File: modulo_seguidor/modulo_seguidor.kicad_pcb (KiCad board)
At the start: 12 copper layers, 100 x 50 mm, 12 parts, among them J1 Battery, J4 Motor Izquierdo, J5 Motor Derecho, J6 puerto sensores, SW1 SW_Push, U1 LM7806_TO220

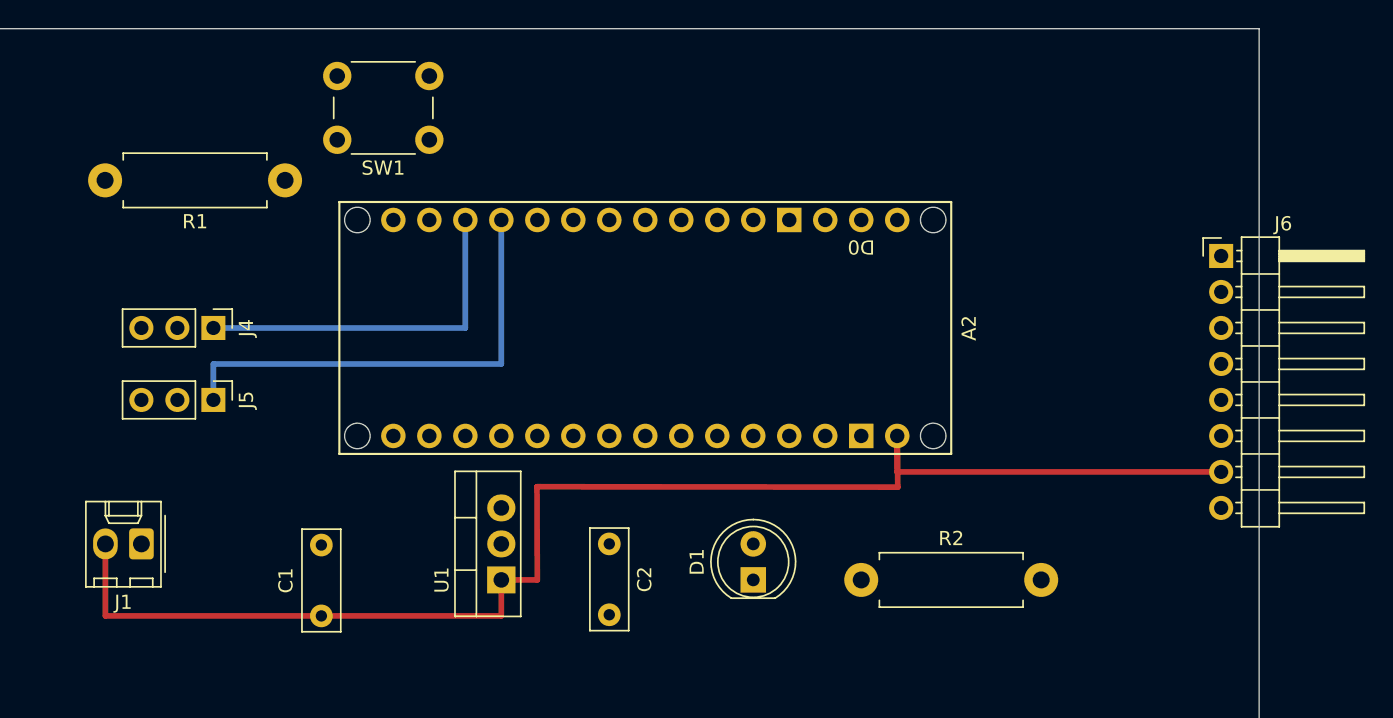
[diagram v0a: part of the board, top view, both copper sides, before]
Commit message: refactor: Cambio las conexiones en los pines del modulo seguidor para compactar la pcb
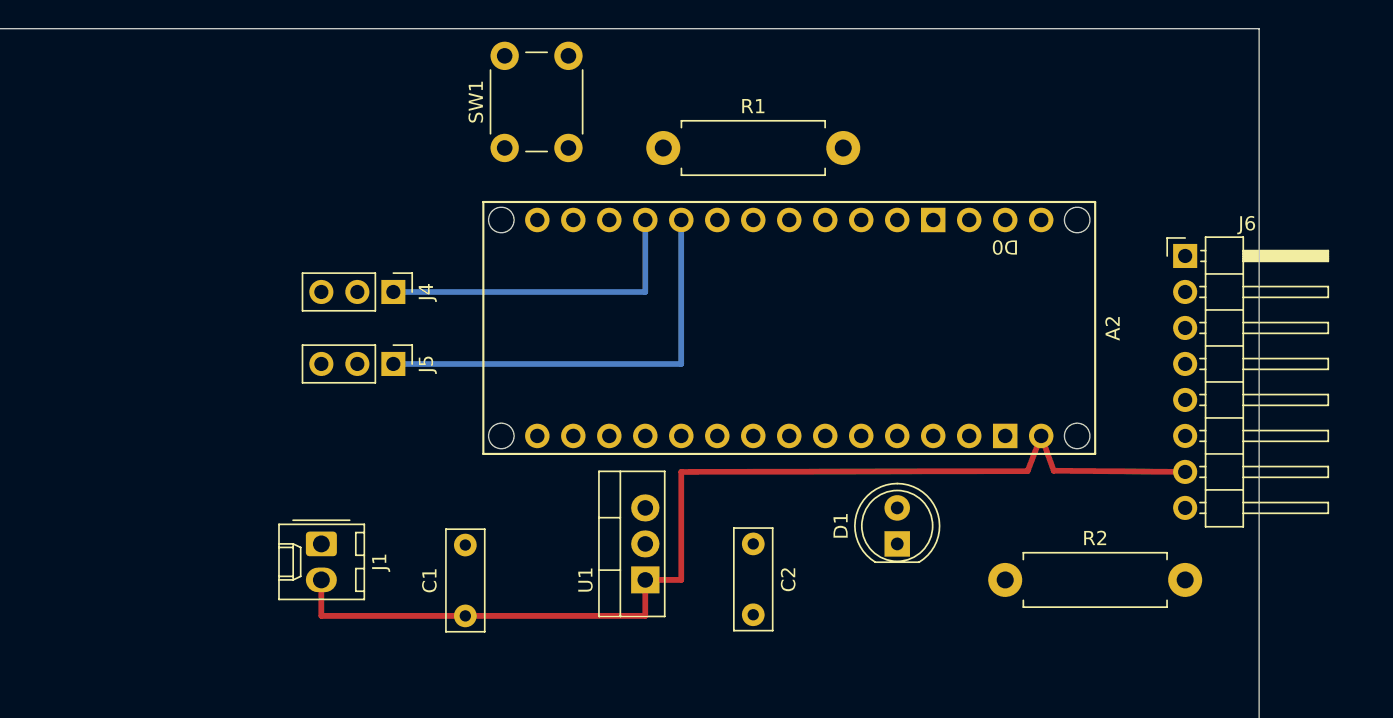
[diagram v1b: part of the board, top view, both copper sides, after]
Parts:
- moved R1 26.8 mm to (108.0, 58.4), turned to 0 degrees
- moved J4 13.0 mm to (88.9, 68.6)
- moved J5 13.0 mm to (88.9, 73.7)
- moved J1 12.7 mm to (83.8, 86.4), turned to -90 degrees
- moved D1 10.5 mm to (124.5, 86.4)
- moved C1 10.2 mm to (94.0, 91.4)
- moved R2 10.2 mm to (132.1, 88.9)
- moved U1 10.2 mm to (106.7, 88.9)
- moved A2 10.2 mm to (95.2, 71.1)
- moved C2 10.2 mm to (114.3, 86.4)
- moved SW1 5.35 mm to (96.8, 58.4), turned to 90 degrees
- moved J6 2.54 mm to (144.8, 66.0)
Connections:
- A2 pad D10: /PWM_IZQ -> /Boton_encendido
- A2 pad D2: /Boton_encendido -> /Sensor6
- A2 pad D3: /Sensor6 -> /Sensor5
- A2 pad D4: /Sensor5 -> /Sensor4
- A2 pad D5: /Sensor4 -> /Sensor3
- A2 pad D6: /Sensor3 -> /Sensor2
- A2 pad D7: /Sensor2 -> /Sensor1
- A2 pad D8: /Sensor1 -> /PWM_DER
- A2 pad D9: /PWM_DER -> /PWM_IZQ
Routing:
- net GND: track 174.9 -> 137.9 mm
- net /Boton_encendido: track 44.6 -> 18.3 mm
- net VCC: track 99.2 -> 77.1 mm
- net /Sensor5: track 42.3 -> 27.0 mm
- net /Sensor6: track 38.1 -> 22.9 mm
- net /Sensor3: track 50.1 -> 35.1 mm
- net /Sensor2: track 54.1 -> 39.2 mm
- net /Sensor4: track 46.1 -> 31.2 mm
- net /Sensor1: track 58.0 -> 43.1 mm
- net Net-(D1-K): track 7.62 -> 10.2 mm
- net Net-(D1-A): track 7.62 -> 5.08 mm
- net /PWM_IZQ: track 25.4 -> 22.9 mm
- net /PWM_DER: track 33.0 -> 30.5 mm
- net +5V: track 60.9 -> 62.6 mm

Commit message: refactor(modulo_seguidor): Intercambio dos pines para hacer los cables más cortos
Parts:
- moved SW1 2.59 mm to (99.3, 58.4)
- moved R1 1.17 mm to (109.1, 58.3)
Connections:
- A2 pad D10: /Boton_encendido -> /PWM_IZQ
- A2 pad D8: /PWM_DER -> /Boton_encendido
- A2 pad D9: /PWM_IZQ -> /PWM_DER
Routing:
- net +5V: track 62.6 -> 65.2 mm
- net /PWM_IZQ: track 22.9 -> 20.3 mm
- net /PWM_DER: track 30.5 -> 27.9 mm
- net /Boton_encendido: track 18.3 -> 17.0 mm
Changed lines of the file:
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@@
 			(layers "*.Cu" "*.Mask")
 			(remove_unused_layers no)
-			(net 22 "/PWM_DER")
+			(net 8 "/Boton_encendido")
 			(pinfunction "D8")
 			(pintype "bidirectional")
@@
 			(layers "*.Cu" "*.Mask")
 			(remove_unused_layers no)
-			(net 4 "/PWM_IZQ")
+			(net 22 "/PWM_DER")
 			(pinfunction "D9")
 			(pintype "bidirectional")
@@
 			(layers "*.Cu" "*.Mask")
 			(remove_unused_layers no)
-			(net 8 "/Boton_encendido")
+			(net 4 "/PWM_IZQ")
 			(pinfunction "D10")
 			(pintype "bidirectional")
@@
 	(footprint "Resistor_THT:R_Axial_DIN0411_L9.9mm_D3.6mm_P12.70mm_Horizontal"
 		(layer "F.Cu")
-		(at 107.95 58.42)
+		(at 109.109289 58.262866)
 		(descr "Resistor, Axial_DIN0411 series, Axial, Horizontal, pin pitch=12.7mm, 1W, length*diameter=9.9*3.6mm^2")
 		(tags "Resistor Axial_DIN0411 series Axial Horizontal pin pitch 12.7mm 1W length 9.9mm diameter 3.6mm")
 		(property "Reference" "R1"
-			(at 6.35 -2.92 360)
+			(at 6.35 -2.92 0)
 			(layer "F.SilkS")
 			(effects
@@
 		)
 		(property "Value" "1k"
-			(at 6.35 2.92 360)
+			(at 6.35 2.92 0)
 			(layer "F.Fab")
 			(effects
@@
 		)
 		(fp_text user "${REFERENCE}"
-			(at 6.35 0 360)
+			(at 6.35 0 0)
 			(layer "F.Fab")
 			(effects
@@
 	(footprint "Button_Switch_THT:SW_PUSH_6mm"
 		(layer "F.Cu")
-		(at 96.756469 58.416841 90)
+		(at 99.35 58.416841 90)
 		(descr "Generic 6mm SW tactile push button")
 		(tags "tact sw push 6mm")
@@
 	)
 	(segment
-		(start 106.68 68.58)
-		(end 106.68 63.5)
+		(start 104.14 68.58)
+		(end 104.14 63.5)
 		(width 0.4)
 		(layer "B.Cu")
@@
 	(segment
 		(start 88.9 68.58)
-		(end 106.68 68.58)
+		(end 104.14 68.58)
 		(width 0.4)
 		(layer "B.Cu")
@@
 	)
 	(segment
-		(start 101.256469 58.416841)
-		(end 101.256469 51.916841)
-		(width 0.4)
-		(layer "In7.Cu")
-		(net 8)
-	)
-	(segment
-		(start 104.14 58.42)
-		(end 101.256469 58.416841)
-		(width 0.4)
-		(layer "In7.Cu")
-		(net 8)
-	)
-	(segment
-		(start 107.95 58.42)
-		(end 104.14 58.431505)
+		(start 109.109289 58.262866)
+		(end 109.22 63.5)
 		(width 0.4)
 		(layer "In7.Cu")
@@
 	)
 	(segment
-		(start 104.14 60.96)
-		(end 104.14 58.42)
+		(start 103.85 58.416841)
+		(end 109.109289 58.262866)
 		(width 0.4)
 		(layer "In7.Cu")
@@
 	)
 	(segment
-		(start 104.14 63.5)
-		(end 104.14 60.96)
+		(start 103.85 51.916841)
+		(end 103.85 58.416841)
 		(width 0.4)
 		(layer "In7.Cu")
@@
 	)
 	(segment
-		(start 109.22 73.66)
-		(end 109.22 63.5)
+		(start 88.9 73.66)
+		(end 106.68 73.66)
 		(width 0.4)
 		(layer "B.Cu")
@@
 	)
 	(segment
-		(start 88.9 73.66)
-		(end 109.22 73.66)
+		(start 106.68 73.66)
+		(end 106.68 63.5)
 		(width 0.4)
 		(layer "B.Cu")
@@
 	)
 	(segment
-		(start 96.756469 51.916841)
-		(end 96.756469 58.416841)
+		(start 127 76.2)
+		(end 127 78.74)
 		(width 0.4)
 		(layer "In10.Cu")
@@
 	)
 	(segment
-		(start 96.756469 58.416841)
-		(end 93.98 58.42)
+		(start 93.98 58.42)
+		(end 93.98 76.2)
 		(width 0.4)
 		(layer "In10.Cu")
@@
 	)
 	(segment
-		(start 93.98 58.42)
-		(end 93.98 76.2)
+		(start 99.35 51.916841)
+		(end 99.35 58.416841)
 		(width 0.4)
 		(layer "In10.Cu")
@@
 	)
 	(segment
-		(start 93.98 76.2)
-		(end 127 76.2)
+		(start 99.35 58.416841)
+		(end 93.98 58.42)
 		(width 0.4)
 		(layer "In10.Cu")
@@
 	)
 	(segment
-		(start 127 76.2)
-		(end 127 78.74)
+		(start 93.98 76.2)
+		(end 127 76.2)
 		(width 0.4)
 		(layer "In10.Cu")

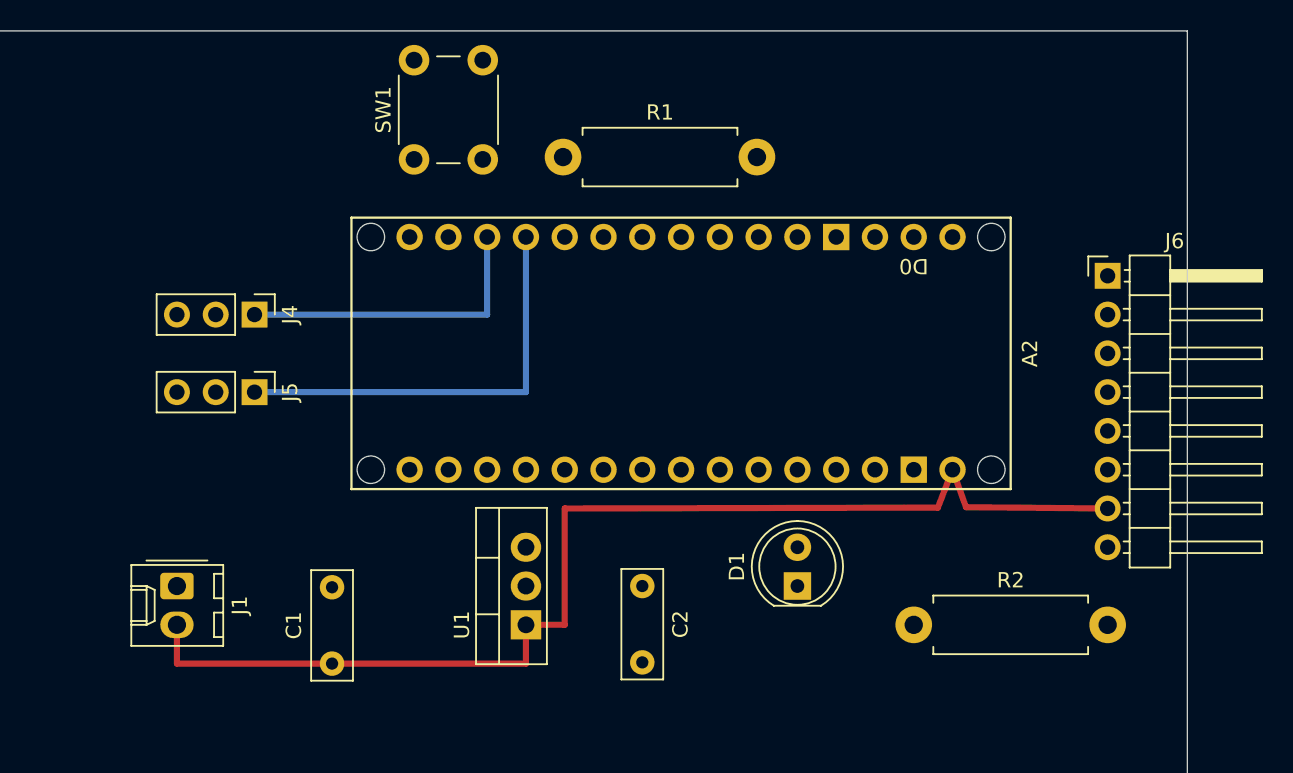
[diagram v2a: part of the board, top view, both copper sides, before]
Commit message: feat(modulo_seguidor): Agrego partes no perforadas y lo referencio en la documentacion
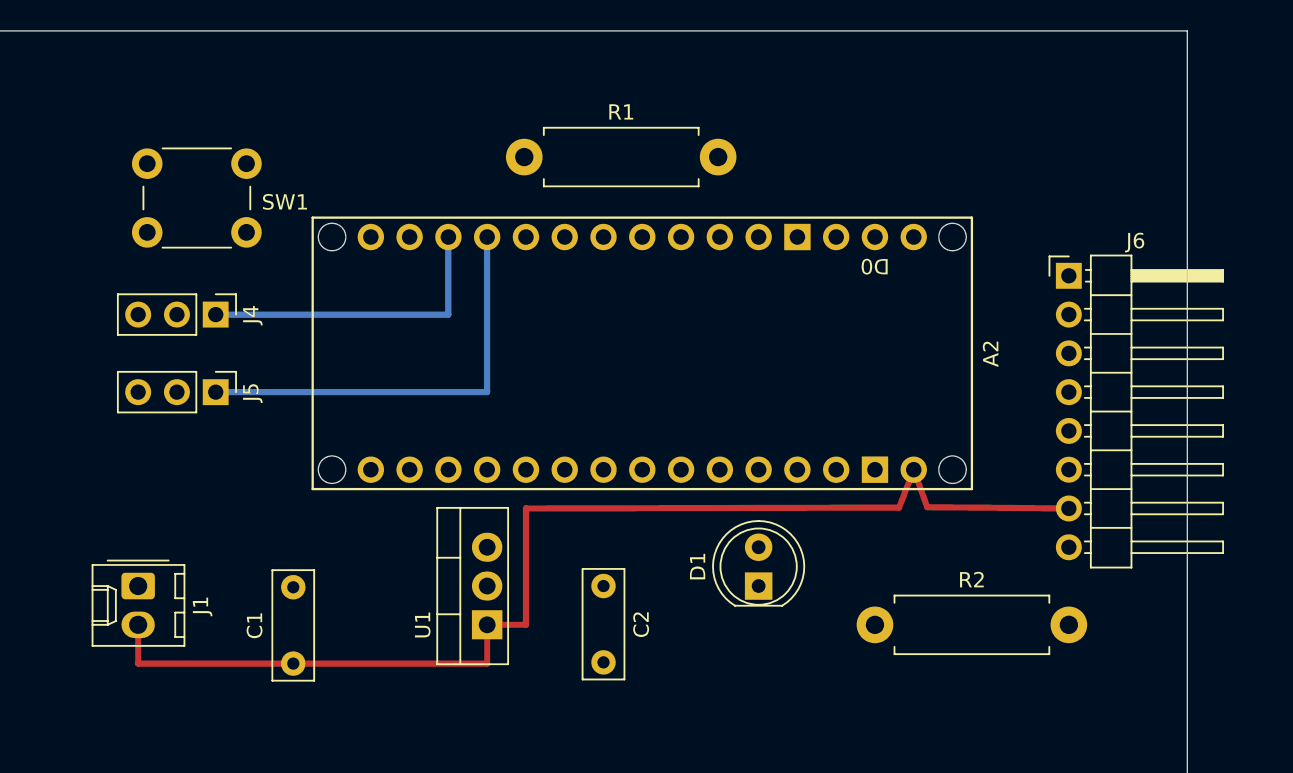
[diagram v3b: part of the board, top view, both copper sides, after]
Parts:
- moved SW1 12.0 mm to (88.4, 63.2), turned to 180 degrees
- moved R2 2.54 mm to (129.5, 88.9)
- moved A2 2.54 mm to (92.7, 71.1)
- moved C1 2.54 mm to (91.4, 91.4)
- moved J4 2.54 mm to (86.4, 68.6)
- moved J5 2.54 mm to (86.4, 73.7)
- moved R1 2.54 mm to (106.6, 58.3)
- moved U1 2.54 mm to (104.1, 88.9)
- moved C2 2.54 mm to (111.8, 86.4)
- moved D1 2.54 mm to (121.9, 86.4)
- moved J1 2.54 mm to (81.3, 86.4)
- moved J6 2.54 mm to (142.2, 66.0)
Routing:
- net /Boton_encendido: track 17.0 -> 29.9 mm
- net +5V: track 65.2 -> 57.8 mm

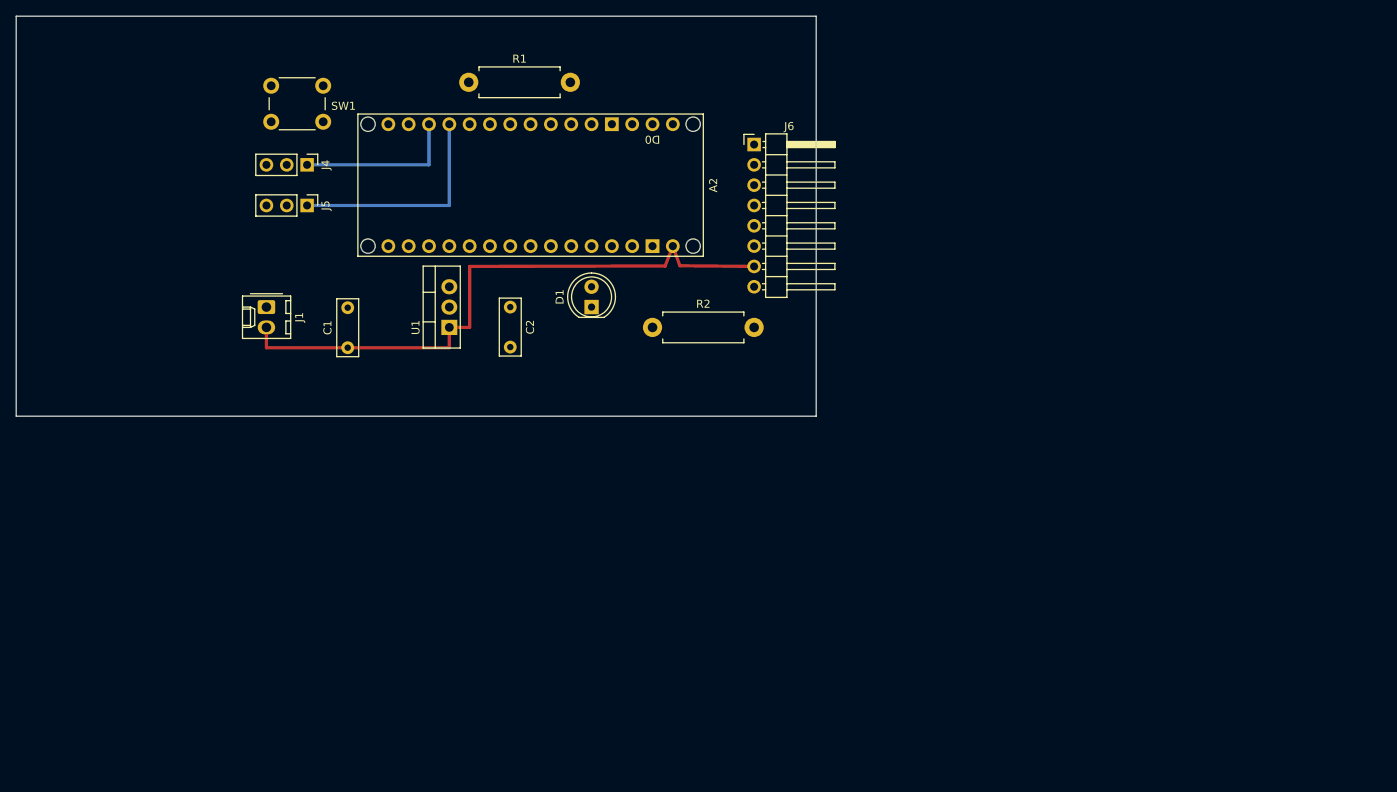
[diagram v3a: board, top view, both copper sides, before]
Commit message: feat(modulo-seguidor): Agrego placa con el seguidor y el puente h incluidos
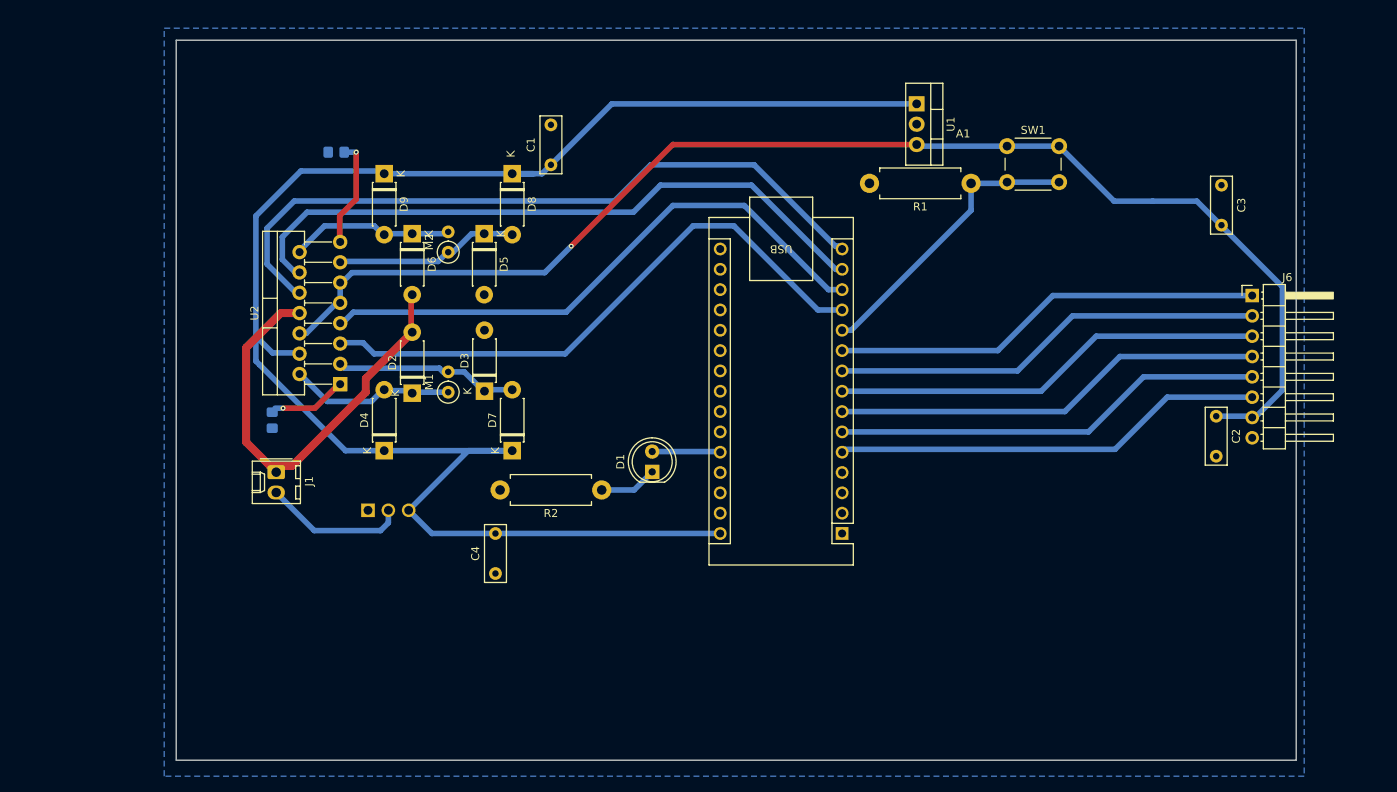
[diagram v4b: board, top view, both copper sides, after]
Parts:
- removed A2: Arduino_Nano_Socket, PCM_arduino-library:Arduino_Nano_Socket
- removed J4: Motor Izquierdo, Connector_PinHeader_2.54mm:PinHeader_1x03_P2.54mm_Vertical
- removed J5: Motor Derecho, Connector_PinHeader_2.54mm:PinHeader_1x03_P2.54mm_Vertical
- added A1: Arduino_Nano_v2.x, Module:Arduino_Nano, F.Cu at (153.2, 114.7)
- added C3: 100nF, Capacitor_THT:C_Disc_D7.0mm_W2.5mm_P5.00mm, F.Cu at (200.7, 71.1)
- added C4: 100nF, Capacitor_THT:C_Disc_D7.0mm_W2.5mm_P5.00mm, F.Cu at (109.9, 119.7)
- added D2: D, Diode_THT:D_DO-41_SOD81_P7.62mm_Horizontal, F.Cu at (99.5, 97.1)
- added D3: D, Diode_THT:D_DO-41_SOD81_P7.62mm_Horizontal, F.Cu at (108.5, 96.9)
- added D4: D, Diode_THT:D_DO-41_SOD81_P7.62mm_Horizontal, F.Cu at (96.0, 104.3)
- added D5: D, Diode_THT:D_DO-41_SOD81_P7.62mm_Horizontal, F.Cu at (108.5, 77.2)
- added D6: D, Diode_THT:D_DO-41_SOD81_P7.62mm_Horizontal, F.Cu at (99.5, 77.2)
- added D7: D, Diode_THT:D_DO-41_SOD81_P7.62mm_Horizontal, F.Cu at (112.0, 104.3)
- added D8: D, Diode_THT:D_DO-41_SOD81_P7.62mm_Horizontal, F.Cu at (112.0, 69.7)
- added D9: D, Diode_THT:D_DO-41_SOD81_P7.62mm_Horizontal, F.Cu at (96.0, 69.7)
- added M1: Motor_IZQ, Resistor_THT:R_Axial_DIN0207_L6.3mm_D2.5mm_P2.54mm_Vertical, F.Cu at (104.0, 97.0)
- added M2: Motor_DER, Resistor_THT:R_Axial_DIN0207_L6.3mm_D2.5mm_P2.54mm_Vertical, F.Cu at (104.0, 79.5)
- added R3: R_US, Resistor_SMD:R_0805_2012Metric_Pad1.20x1.40mm_HandSolder, B.Cu at (82.0, 100.5)
- added R4: R_US, Resistor_SMD:R_0805_2012Metric_Pad1.20x1.40mm_HandSolder, B.Cu at (90.0, 67.0)
- added SW2: SW_Nidec_CAS-120A1, Converter_DCDC:Converter_DCDC_TRACO_TSR2-xxxx_THT, B.Cu at (94.0, 111.8)
- added U2: L298N, Package_TO_SOT_THT:TO-220-15_P2.54x5.08mm_StaggerOdd_Lead4.58mm_Vertical, F.Cu at (90.5, 96.0)
- moved C2 89.3 mm to (200.0, 100.0)
- moved SW1 85.5 mm to (173.9, 66.2), turned to 0 degrees
- moved J6 65.1 mm to (204.5, 84.9)
- moved U1 64.8 mm to (162.6, 61.0), turned to -90 degrees
- moved R1 64.0 mm to (169.4, 70.9), turned to 180 degrees
- moved C1 34.2 mm to (116.8, 68.6)
- moved D1 22.0 mm to (129.5, 107.0)
- moved R2 21.3 mm to (123.2, 109.2), turned to 180 degrees
- moved J1 20.7 mm to (82.5, 107.0)
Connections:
- C2 pad 1: /Salida Regulador -> Salida Regulador
- J1 pad 2: VCC -> Net-(J1-Pin_2)
- J6 pad 7: VCC -> Salida Regulador
- SW1 pad 1: +5V -> Salida Regulador
- U1 pad 3: /Salida Regulador -> Salida Regulador
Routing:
- net Salida Regulador: track 0.00 -> 164.2 mm, vias 0 -> 1
- net VCC: track 77.1 -> 208.5 mm
- net /Entrada PWM Motor B: track 0.00 -> 89.4 mm
- net /Entrada DIG Motor B: track 0.00 -> 82.5 mm
- net GND: track 137.9 -> 56.5 mm
- net /Entrada PWM Motor A: track 0.00 -> 74.4 mm
- net /Entrada DIG Motor A: track 0.00 -> 73.2 mm
- net +5V: track 57.8 -> 0.00 mm
- net /Salida Regulador: track 45.7 -> 0.00 mm
- net /Sensor6: track 22.9 -> 54.1 mm
- net /PWM_DER: track 27.9 -> 0.00 mm
- net /Sensor5: track 27.0 -> 54.1 mm
- net /Sensor4: track 31.2 -> 54.1 mm
- net Net-(D5-K): track 0.00 -> 22.9 mm
- net Net-(D3-K): track 0.00 -> 22.9 mm
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- added copper zone on B.Cu, net GND
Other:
- board size 100 x 50 mm -> 140 x 90 mm
- copper layers 12 -> 2
